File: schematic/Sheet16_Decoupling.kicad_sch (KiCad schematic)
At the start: 11 parts

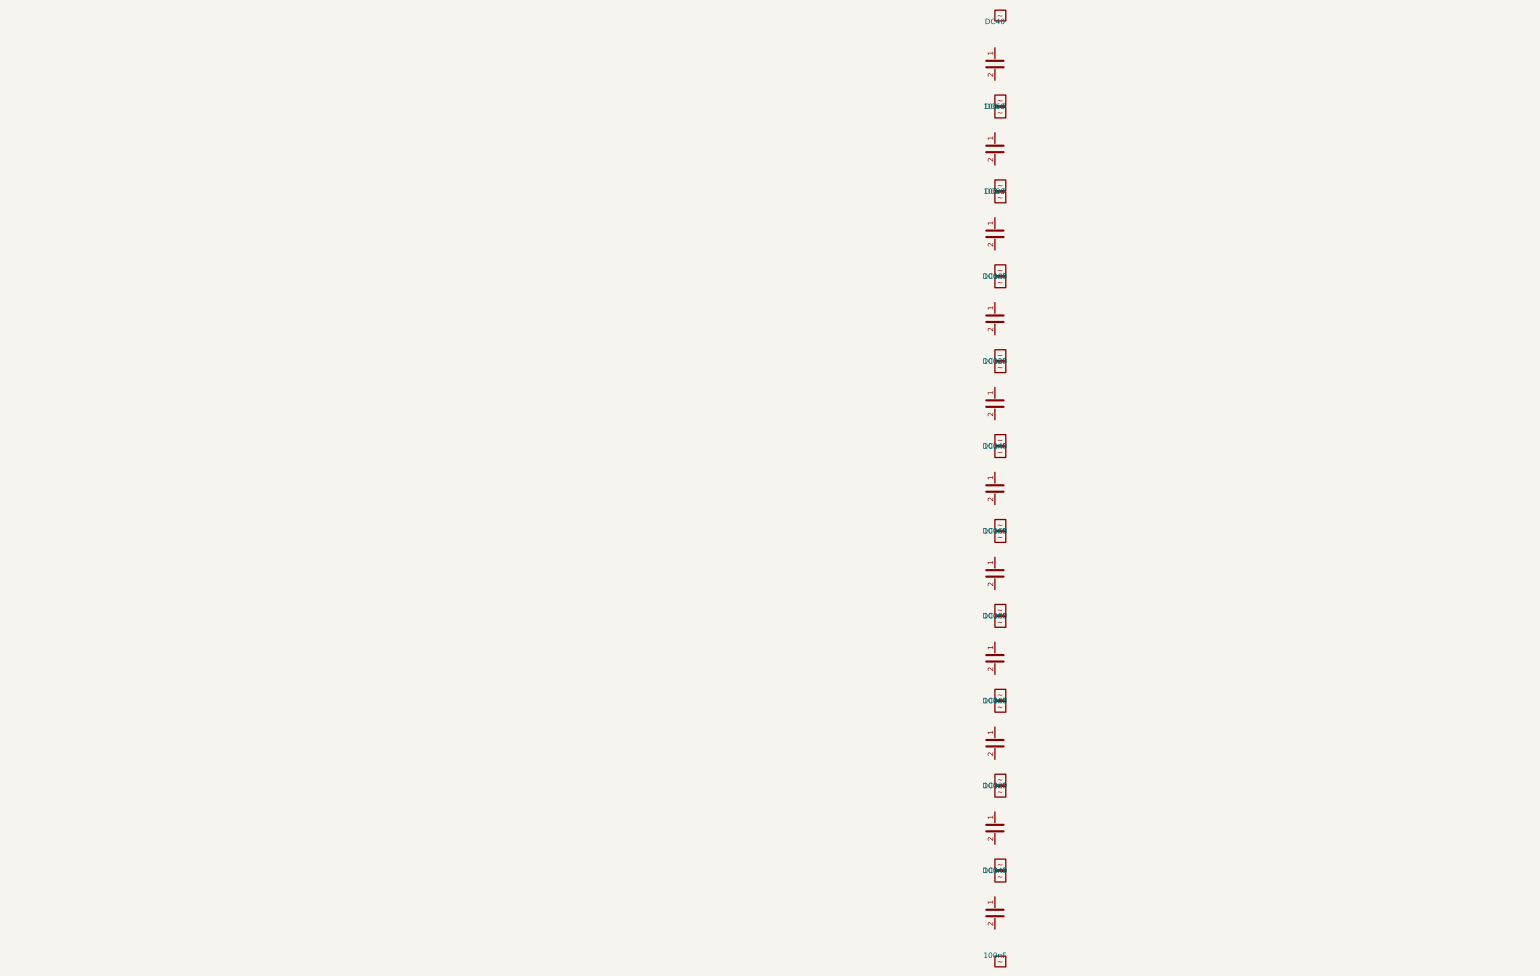
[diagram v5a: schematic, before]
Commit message: feat: connect ALL passive components and fix clock routing
- Added PASSIVE_TOPOLOGY dict mapping 139 passives to their nets
- Passive pin endpoints now get global_labels (was 0 connected, now 138)
- R38 intentionally GND-GND (RECAL_EN pull-down)
- Fixed LMK clock output mapping: CLKout0→ADC_CLK_P, CLKout2→FPGA_REFCLK_P, etc.
- Fixed TPS7H5001-SP SYNC pin collision with LMX_SYNC
- Total connections: 867 pins (up from 641)
- Cross-sheet nets: 52
- Power rails: VIN(33), +3V3(98), GND(228) all with decoupling
- JESD204C: U1↔U2 on 4 lanes ✓
- SPI: U1↔U2↔U3↔U4 ✓
- Clock: LMK→ADC (CLK+SYSREF), LMK→FPGA (REF+SPW) ✓
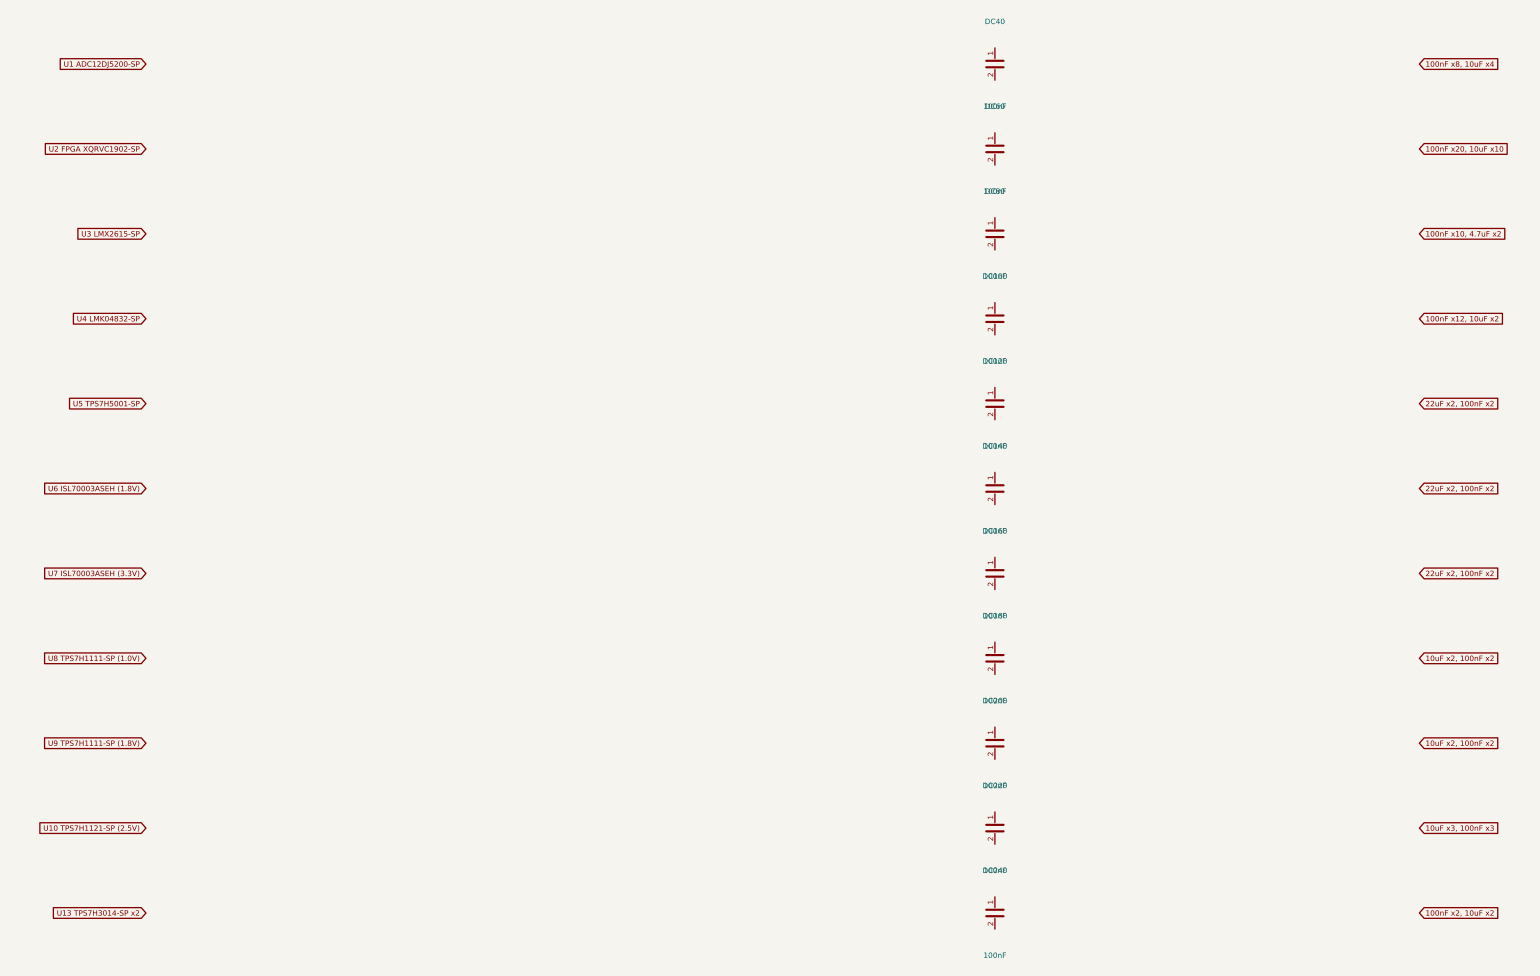
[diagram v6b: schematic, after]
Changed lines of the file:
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@@
     (pin "1")
     (pin "2")
-  )      (symbol (lib_id "Device:C") (at 280 60 0) (unit 1)
+  )  (global_label "U1 ADC12DJ5200-SP" (shape input) (at 80 40 180) (effects (font (size 1.27 1.27)) (justify right)))  (global_label "100nF x8, 10uF x4" (shape input) (at 380 40 0) (effects (font (size 1.27 1.27)) (justify left)))  (symbol (lib_id "Device:C") (at 280 60 0) (unit 1)
     (in_bom yes) (on_board yes)
     (property "Reference" "DC60" (at 280 50 0) (effects (font (size 1.27 1.27))))
@@
     (pin "1")
     (pin "2")
-  )      (symbol (lib_id "Device:C") (at 280 80 0) (unit 1)
+  )  (global_label "U2 FPGA XQRVC1902-SP" (shape input) (at 80 60 180) (effects (font (size 1.27 1.27)) (justify right)))  (global_label "100nF x20, 10uF x10" (shape input) (at 380 60 0) (effects (font (size 1.27 1.27)) (justify left)))  (symbol (lib_id "Device:C") (at 280 80 0) (unit 1)
     (in_bom yes) (on_board yes)
     (property "Reference" "DC80" (at 280 70 0) (effects (font (size 1.27 1.27))))
@@
     (pin "1")
     (pin "2")
-  )      (symbol (lib_id "Device:C") (at 280 100 0) (unit 1)
+  )  (global_label "U3 LMX2615-SP" (shape input) (at 80 80 180) (effects (font (size 1.27 1.27)) (justify right)))  (global_label "100nF x10, 4.7uF x2" (shape input) (at 380 80 0) (effects (font (size 1.27 1.27)) (justify left)))  (symbol (lib_id "Device:C") (at 280 100 0) (unit 1)
     (in_bom yes) (on_board yes)
     (property "Reference" "DC100" (at 280 90 0) (effects (font (size 1.27 1.27))))
@@
     (pin "1")
     (pin "2")
-  )      (symbol (lib_id "Device:C") (at 280 120 0) (unit 1)
+  )  (global_label "U4 LMK04832-SP" (shape input) (at 80 100 180) (effects (font (size 1.27 1.27)) (justify right)))  (global_label "100nF x12, 10uF x2" (shape input) (at 380 100 0) (effects (font (size 1.27 1.27)) (justify left)))  (symbol (lib_id "Device:C") (at 280 120 0) (unit 1)
     (in_bom yes) (on_board yes)
     (property "Reference" "DC120" (at 280 110 0) (effects (font (size 1.27 1.27))))
@@
     (pin "1")
     (pin "2")
-  )      (symbol (lib_id "Device:C") (at 280 140 0) (unit 1)
+  )  (global_label "U5 TPS7H5001-SP" (shape input) (at 80 120 180) (effects (font (size 1.27 1.27)) (justify right)))  (global_label "22uF x2, 100nF x2" (shape input) (at 380 120 0) (effects (font (size 1.27 1.27)) (justify left)))  (symbol (lib_id "Device:C") (at 280 140 0) (unit 1)
     (in_bom yes) (on_board yes)
     (property "Reference" "DC140" (at 280 130 0) (effects (font (size 1.27 1.27))))
@@
     (pin "1")
     (pin "2")
-  )      (symbol (lib_id "Device:C") (at 280 160 0) (unit 1)
+  )  (global_label "U6 ISL70003ASEH (1.8V)" (shape input) (at 80 140 180) (effects (font (size 1.27 1.27)) (justify right)))  (global_label "22uF x2, 100nF x2" (shape input) (at 380 140 0) (effects (font (size 1.27 1.27)) (justify left)))  (symbol (lib_id "Device:C") (at 280 160 0) (unit 1)
     (in_bom yes) (on_board yes)
     (property "Reference" "DC160" (at 280 150 0) (effects (font (size 1.27 1.27))))
@@
     (pin "1")
     (pin "2")
-  )      (symbol (lib_id "Device:C") (at 280 180 0) (unit 1)
+  )  (global_label "U7 ISL70003ASEH (3.3V)" (shape input) (at 80 160 180) (effects (font (size 1.27 1.27)) (justify right)))  (global_label "22uF x2, 100nF x2" (shape input) (at 380 160 0) (effects (font (size 1.27 1.27)) (justify left)))  (symbol (lib_id "Device:C") (at 280 180 0) (unit 1)
     (in_bom yes) (on_board yes)
     (property "Reference" "DC180" (at 280 170 0) (effects (font (size 1.27 1.27))))
@@
     (pin "1")
     (pin "2")
-  )      (symbol (lib_id "Device:C") (at 280 200 0) (unit 1)
+  )  (global_label "U8 TPS7H1111-SP (1.0V)" (shape input) (at 80 180 180) (effects (font (size 1.27 1.27)) (justify right)))  (global_label "10uF x2, 100nF x2" (shape input) (at 380 180 0) (effects (font (size 1.27 1.27)) (justify left)))  (symbol (lib_id "Device:C") (at 280 200 0) (unit 1)
     (in_bom yes) (on_board yes)
     (property "Reference" "DC200" (at 280 190 0) (effects (font (size 1.27 1.27))))
@@
     (pin "1")
     (pin "2")
-  )      (symbol (lib_id "Device:C") (at 280 220 0) (unit 1)
+  )  (global_label "U9 TPS7H1111-SP (1.8V)" (shape input) (at 80 200 180) (effects (font (size 1.27 1.27)) (justify right)))  (global_label "10uF x2, 100nF x2" (shape input) (at 380 200 0) (effects (font (size 1.27 1.27)) (justify left)))  (symbol (lib_id "Device:C") (at 280 220 0) (unit 1)
     (in_bom yes) (on_board yes)
     (property "Reference" "DC220" (at 280 210 0) (effects (font (size 1.27 1.27))))
@@
     (pin "1")
     (pin "2")
-  )      (symbol (lib_id "Device:C") (at 280 240 0) (unit 1)
+  )  (global_label "U10 TPS7H1121-SP (2.5V)" (shape input) (at 80 220 180) (effects (font (size 1.27 1.27)) (justify right)))  (global_label "10uF x3, 100nF x3" (shape input) (at 380 220 0) (effects (font (size 1.27 1.27)) (justify left)))  (symbol (lib_id "Device:C") (at 280 240 0) (unit 1)
     (in_bom yes) (on_board yes)
     (property "Reference" "DC240" (at 280 230 0) (effects (font (size 1.27 1.27))))
@@
     (pin "1")
     (pin "2")
-  )
-  (global_label "~" (at 280.0000 28.5700 0) (effects (font (size 1.27 1.27))))
-  (global_label "~" (at 280.0000 51.4300 0) (effects (font (size 1.27 1.27))))
-  (global_label "~" (at 280.0000 48.5700 0) (effects (font (size 1.27 1.27))))
-  (global_label "~" (at 280.0000 71.4300 0) (effects (font (size 1.27 1.27))))
-  (global_label "~" (at 280.0000 68.5700 0) (effects (font (size 1.27 1.27))))
-  (global_label "~" (at 280.0000 91.4300 0) (effects (font (size 1.27 1.27))))
-  (global_label "~" (at 280.0000 88.5700 0) (effects (font (size 1.27 1.27))))
-  (global_label "~" (at 280.0000 111.4300 0) (effects (font (size 1.27 1.27))))
-  (global_label "~" (at 280.0000 108.5700 0) (effects (font (size 1.27 1.27))))
-  (global_label "~" (at 280.0000 131.4300 0) (effects (font (size 1.27 1.27))))
-  (global_label "~" (at 280.0000 128.5700 0) (effects (font (size 1.27 1.27))))
-  (global_label "~" (at 280.0000 151.4300 0) (effects (font (size 1.27 1.27))))
-  (global_label "~" (at 280.0000 148.5700 0) (effects (font (size 1.27 1.27))))
-  (global_label "~" (at 280.0000 171.4300 0) (effects (font (size 1.27 1.27))))
-  (global_label "~" (at 280.0000 168.5700 0) (effects (font (size 1.27 1.27))))
-  (global_label "~" (at 280.0000 191.4300 0) (effects (font (size 1.27 1.27))))
-  (global_label "~" (at 280.0000 188.5700 0) (effects (font (size 1.27 1.27))))
-  (global_label "~" (at 280.0000 211.4300 0) (effects (font (size 1.27 1.27))))
-  (global_label "~" (at 280.0000 208.5700 0) (effects (font (size 1.27 1.27))))
-  (global_label "~" (at 280.0000 231.4300 0) (effects (font (size 1.27 1.27))))
-  (global_label "~" (at 280.0000 228.5700 0) (effects (font (size 1.27 1.27))))
-  (global_label "~" (at 280.0000 251.4300 0) (effects (font (size 1.27 1.27))))
-  (sheet_instances (path "/" (page "1")))
+  )  (global_label "U13 TPS7H3014-SP x2" (shape input) (at 80 240 180) (effects (font (size 1.27 1.27)) (justify right)))  (global_label "100nF x2, 10uF x2" (shape input) (at 380 240 0) (effects (font (size 1.27 1.27)) (justify left)))  (sheet_instances (path "/" (page "1")))
 )
